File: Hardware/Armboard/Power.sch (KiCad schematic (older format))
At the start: 22 parts

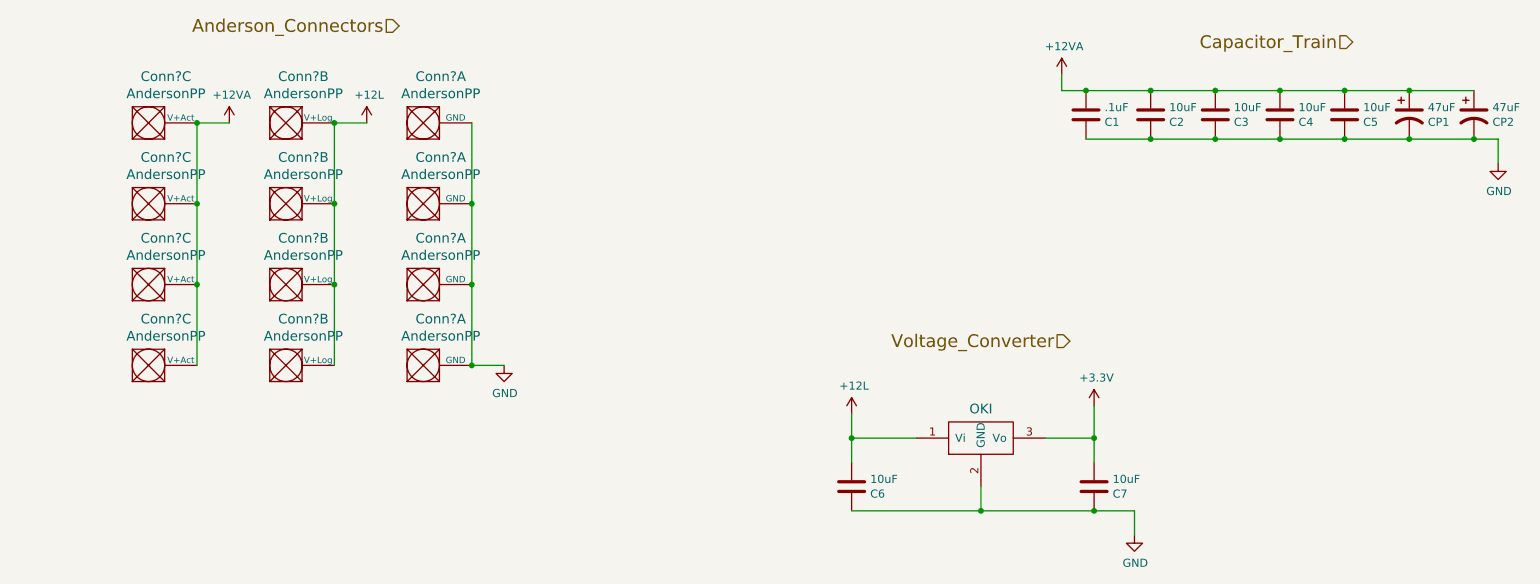
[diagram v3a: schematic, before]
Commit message: Put Anderson connectors on front page, replaced OKI with Buckman converter
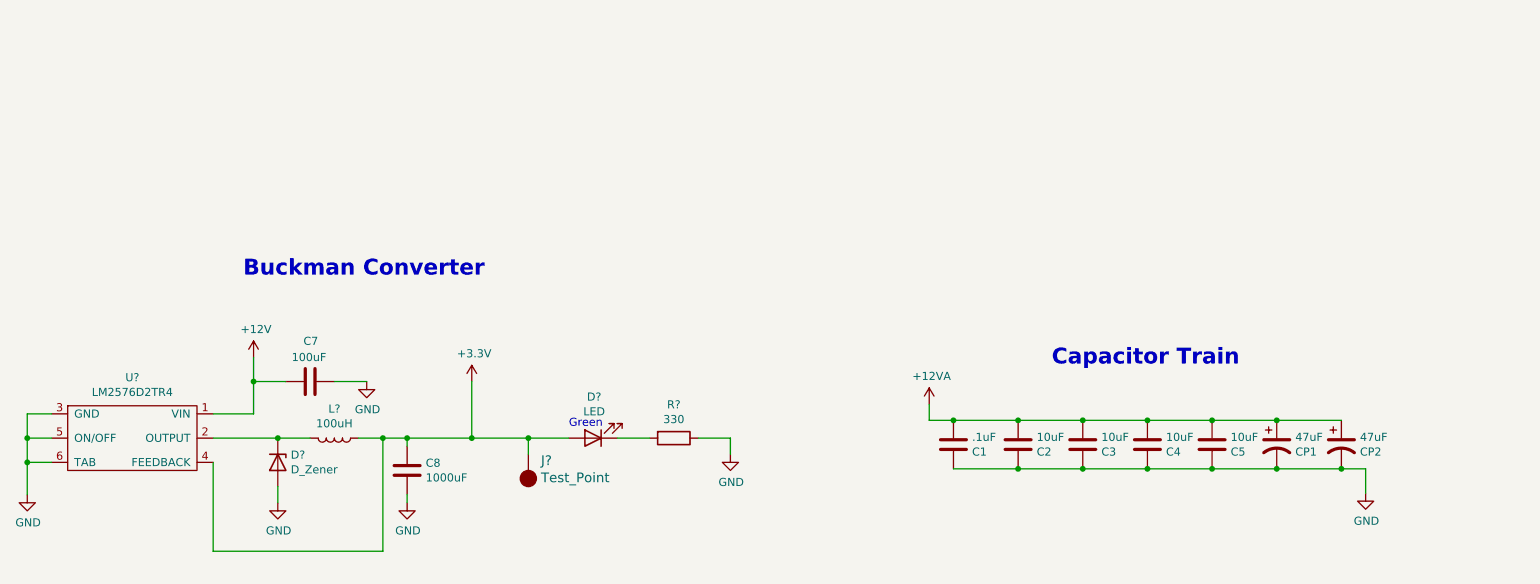
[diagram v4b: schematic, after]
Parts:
- removed 10uF: C6, symbol Device:C
- removed 10uF: C7, symbol Device:C
- removed Conn? (x12): AndersonPP, symbol Armboard-rescue:AndersonPP-MRDT_Connectors
- removed U?: OKI, symbol MRDT_Devices:OKI
- added C7: 100uF, symbol Device:C
- added C8: 1000uF, symbol Device:C
- added D?: D_Zener, symbol Device:D_Zener
- added D?: LED, symbol Device:LED
- added J?: Test_Point, symbol MRDT_Connectors:Test_Point
- added L?: 100uH, symbol Device:L
- added R?: 330, symbol Device:R
- added U?: LM2576D2TR4, symbol MRDT_Devices:LM2576D2TR4
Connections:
- net +3V3: now also C8.1, D?.2 (A), J?.1, L?.1, U?.4 (FEEDBACK)
- net GND: now also C7.2, C8.2, D?.2 (A), R?.1, U?.3 (GND), U?.5 (ON/OFF), U?.6 (TAB)
- new net: D?.1 (K), L?.2, U?.2 (OUTPUT)
- new net: D?.1 (K), R?.2
- new net +12V: C7.1, U?.1 (VIN)
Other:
- note added: "Buckman Converter"
- note added: "Capacitor Train"
- note added: "Green"
- moved on the sheet: .1uF, 10uF, 47uF
